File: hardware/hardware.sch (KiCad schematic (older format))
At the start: 16 parts, among them J1 power in, J2 cell case, J3 P1, U1 MIC5205-3.3YM5

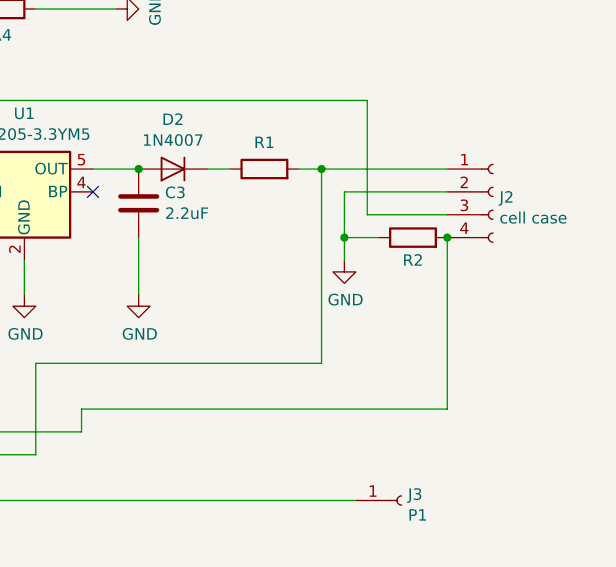
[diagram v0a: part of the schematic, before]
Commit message: add min and max temp and voltage values
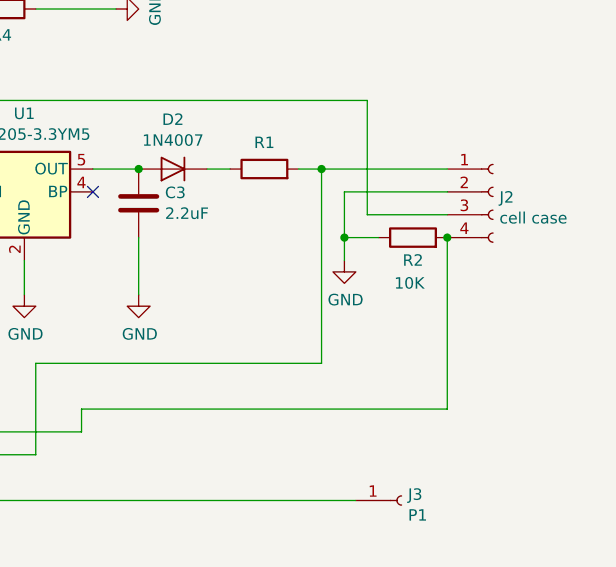
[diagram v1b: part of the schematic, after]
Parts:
- R2: value R -> 10K
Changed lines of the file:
@@
 P 6300 2700
 F 0 "R2" V 6200 2700 50  0000 C CNN
-F 1 "R" H 6370 2655 50  0001 L CNN
+F 1 "10K" V 6100 2650 50  0000 L CNN
 F 2 "Resistor_SMD:R_1206_3216Metric" V 6230 2700 50  0001 C CNN
 F 3 "~" H 6300 2700 50  0001 C CNN
